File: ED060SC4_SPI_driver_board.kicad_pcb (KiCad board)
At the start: 4 copper layers, 71.2 x 49 mm, 82 parts, among them J1 ED060SC4, J2 Conn_01x06, J3 Conn_01x04, J4 Conn_01x04, J5 Conn_01x06, J6 Conn_01x02, SW1 SS12D07VG2, SW2 DSIC01LSGET, U1 TPS65185RGZR, U2 STM32F103C8T6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

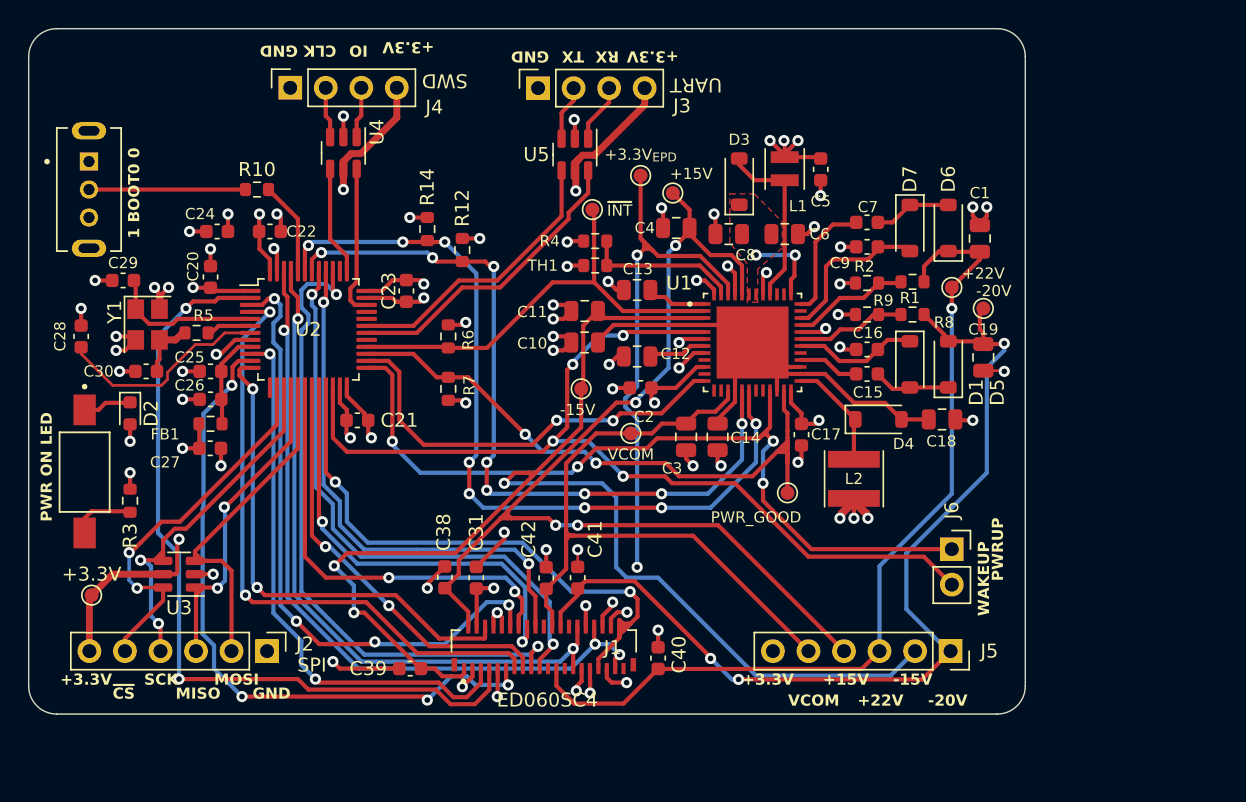
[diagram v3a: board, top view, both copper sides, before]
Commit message: Updated TPS pad for heat dissipation
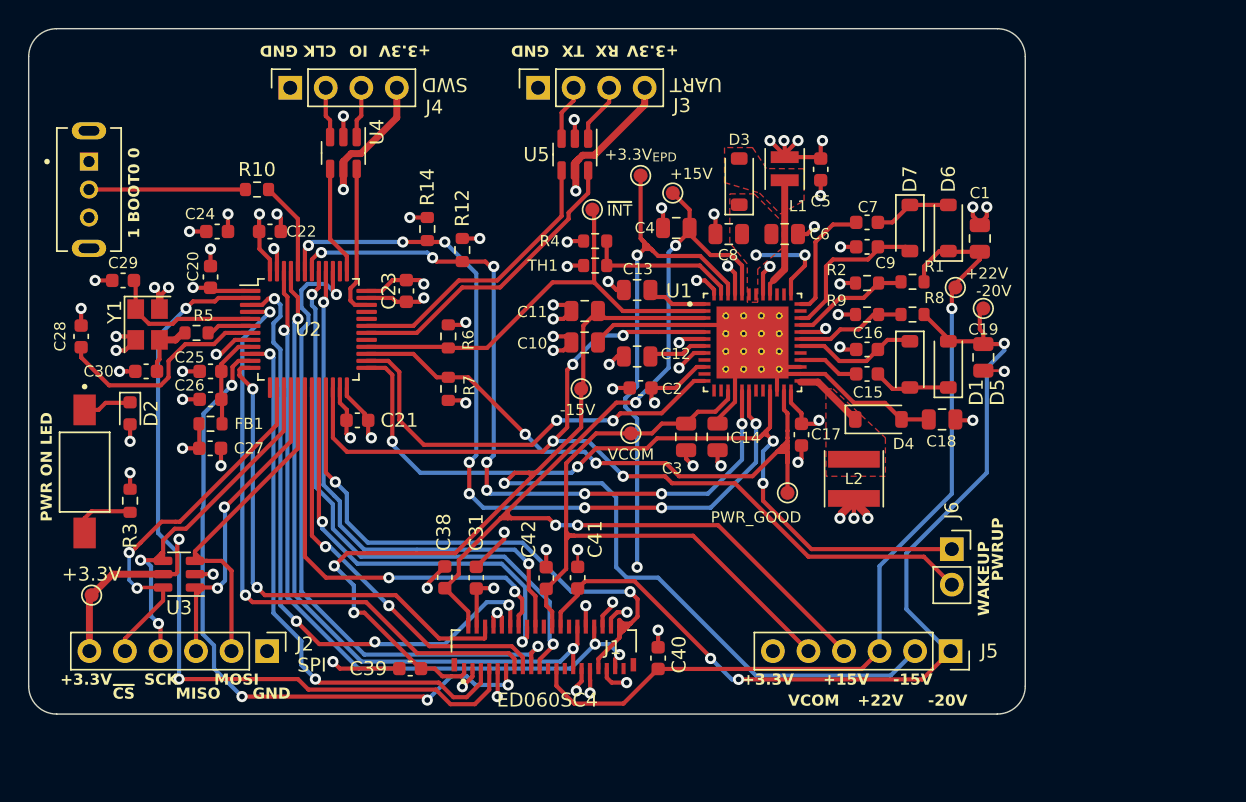
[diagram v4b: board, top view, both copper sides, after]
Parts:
- moved TP5 0.25 mm to (114.2, 65.5)
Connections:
- net /PWR_ON_LED renamed /PWR_ON_LED_0
- net Net-(R3-Pad1) renamed /PWR_ON_LED_1
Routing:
- net /EPD Power Rails/VB_SW: track 12.8 -> 8.60 mm
- net /EPD Power Rails/VN_SW: track 7.95 -> 5.16 mm
- net +3.3V: track 80.1 -> 81.4 mm, vias 20 -> 21
- net /EPD Power Rails/VB: track 5.74 -> 6.73 mm
- net /NRST: track 15.3 -> 15.9 mm
- net GND: track 106.4 -> 107.0 mm
- added copper zone on F.Cu, net /EPD Power Rails/VB_SW
- added copper zone on F.Cu, net /EPD Power Rails/VN_SW

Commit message: Smaller board outline and some silkscreen info
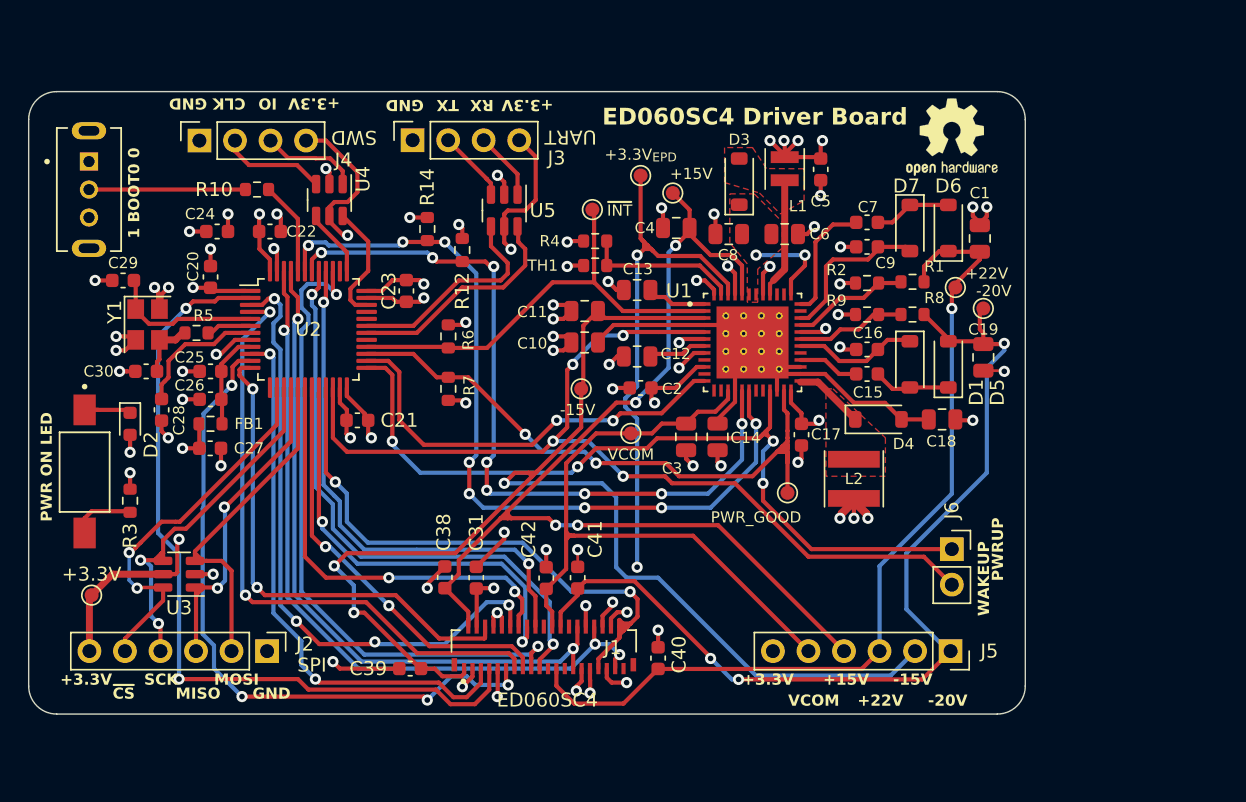
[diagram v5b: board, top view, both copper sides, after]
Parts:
- added REF**: OSHW-Logo2_7.3x6mm_SilkScreen, Symbol:OSHW-Logo2_7.3x6mm_SilkScreen, F.Cu at (114.0, 54.8)
- moved J3 9.72 mm to (75.5, 55.0)
- moved C28 7.79 mm to (57.5, 74.2), turned to 90 degrees
- moved J4 7.51 mm to (60.2, 55.0)
- moved U5 6.44 mm to (82.0, 60.0)
- moved U4 3.51 mm to (69.5, 59.2)
- moved D2 0.75 mm to (55.2, 75.2)
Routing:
- net /NRST: track 15.9 -> 9.60 mm
- net /USART1_RX: track 21.9 -> 16.4 mm
- net /USART1_TX: track 20.5 -> 15.5 mm
- net /SWCLK_conn: track 3.65 -> 7.53 mm
- net /SWDIO_conn: track 3.66 -> 7.00 mm
- net /SWCLK: track 7.81 -> 4.86 mm
- net /SWDIO: track 10.9 -> 8.60 mm
- net /USART1_TX_conn: track 3.97 -> 5.15 mm
- net +3.3V: track 81.4 -> 82.6 mm
- net /PWR_ON_LED_0: track 3.47 -> 4.33 mm
- net /USART1_RX_conn: track 4.23 -> 4.89 mm
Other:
- board size 71.2 x 49 mm -> 71.2 x 44.5 mm
- board text added: "ED060SC4 Driver Board"
- board text added: "Revision 1"
- board text added: "design by hatrix"

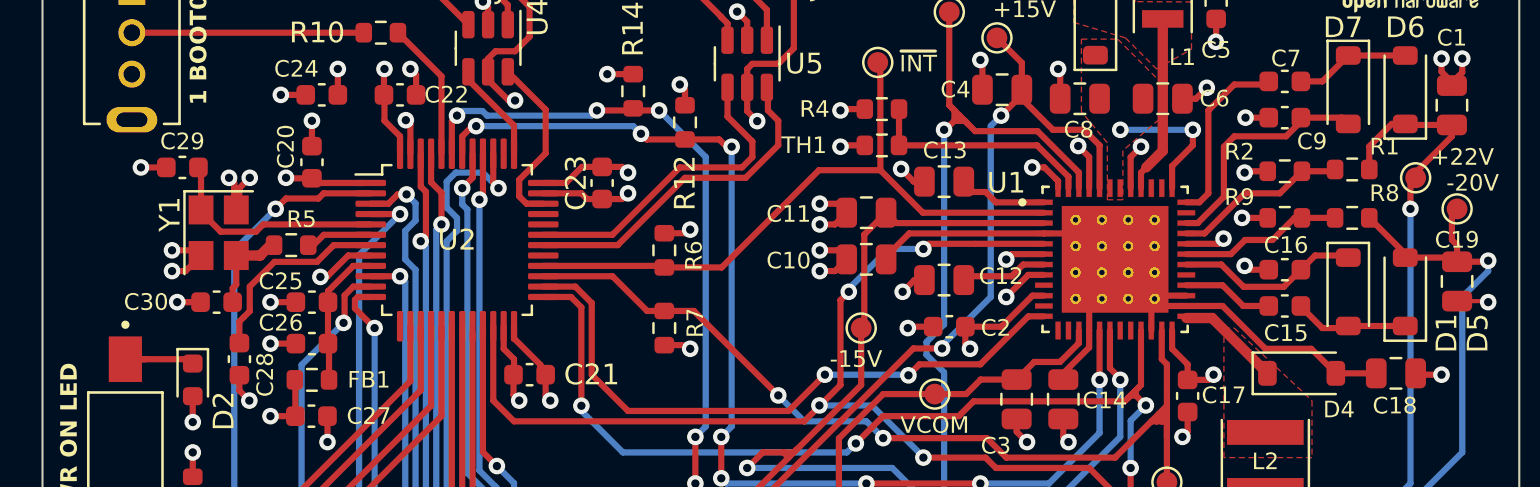
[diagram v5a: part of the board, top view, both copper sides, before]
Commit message: bigger via holes for TPS heat
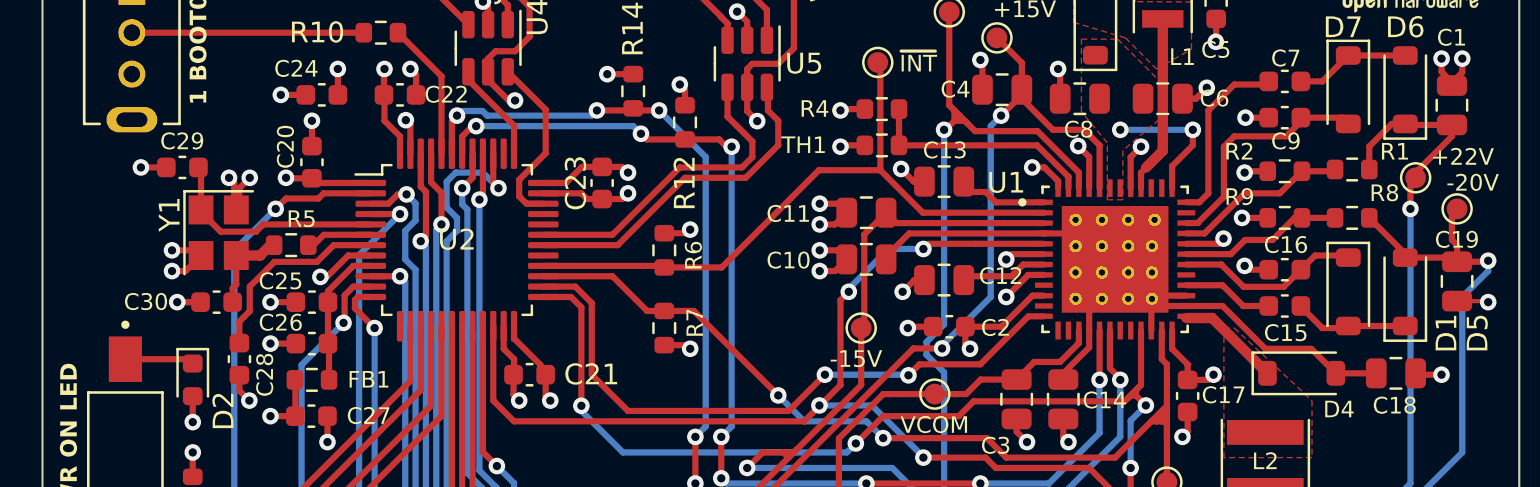
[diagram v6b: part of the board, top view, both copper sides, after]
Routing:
- net /PWR_ON_LED_0: track 4.33 -> 3.34 mm
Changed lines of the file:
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@@
     (pad "48" smd roundrect (at -2.75 -3.435 90) (size 0.86 0.26) (layers "F.Cu" "F.Paste" "F.Mask") (roundrect_rratio 0.03)
       (net 1 "GND") (pinfunction "AGND2") (pintype "power_in"))
-    (pad "49" thru_hole circle (at -1.905 -1.905) (size 0.508 0.508) (drill 0.254) (layers "*.Cu" "*.Mask")
+    (pad "49" thru_hole circle (at -1.905 -1.905) (size 0.6 0.6) (drill 0.3) (layers "*.Cu" "*.Mask")
       (net 77 "/EPD Power Rails/VN") (pinfunction "SUBSTRATE") (pintype "bidirectional"))
-    (pad "49" thru_hole circle (at -1.905 -0.635) (size 0.508 0.508) (drill 0.254) (layers "*.Cu" "*.Mask")
+    (pad "49" thru_hole circle (at -1.905 -0.635) (size 0.6 0.6) (drill 0.3) (layers "*.Cu" "*.Mask")
       (net 77 "/EPD Power Rails/VN") (pinfunction "SUBSTRATE") (pintype "bidirectional"))
-    (pad "49" thru_hole circle (at -1.905 0.635) (size 0.508 0.508) (drill 0.254) (layers "*.Cu" "*.Mask")
+    (pad "49" thru_hole circle (at -1.905 0.635) (size 0.6 0.6) (drill 0.3) (layers "*.Cu" "*.Mask")
       (net 77 "/EPD Power Rails/VN") (pinfunction "SUBSTRATE") (pintype "bidirectional"))
-    (pad "49" thru_hole circle (at -1.905 1.905) (size 0.508 0.508) (drill 0.254) (layers "*.Cu" "*.Mask")
+    (pad "49" thru_hole circle (at -1.905 1.905) (size 0.6 0.6) (drill 0.3) (layers "*.Cu" "*.Mask")
       (net 77 "/EPD Power Rails/VN") (pinfunction "SUBSTRATE") (pintype "bidirectional"))
-    (pad "49" thru_hole circle (at -0.635 -1.905) (size 0.508 0.508) (drill 0.254) (layers "*.Cu" "*.Mask")
+    (pad "49" thru_hole circle (at -0.635 -1.905) (size 0.6 0.6) (drill 0.3) (layers "*.Cu" "*.Mask")
       (net 77 "/EPD Power Rails/VN") (pinfunction "SUBSTRATE") (pintype "bidirectional"))
-    (pad "49" thru_hole circle (at -0.635 -0.635) (size 0.508 0.508) (drill 0.254) (layers "*.Cu" "*.Mask")
+    (pad "49" thru_hole circle (at -0.635 -0.635) (size 0.6 0.6) (drill 0.3) (layers "*.Cu" "*.Mask")
       (net 77 "/EPD Power Rails/VN") (pinfunction "SUBSTRATE") (pintype "bidirectional"))
-    (pad "49" thru_hole circle (at -0.635 0.635) (size 0.508 0.508) (drill 0.254) (layers "*.Cu" "*.Mask")
+    (pad "49" thru_hole circle (at -0.635 0.635) (size 0.6 0.6) (drill 0.3) (layers "*.Cu" "*.Mask")
       (net 77 "/EPD Power Rails/VN") (pinfunction "SUBSTRATE") (pintype "bidirectional"))
-    (pad "49" thru_hole circle (at -0.635 1.905) (size 0.508 0.508) (drill 0.254) (layers "*.Cu" "*.Mask")
+    (pad "49" thru_hole circle (at -0.635 1.905) (size 0.6 0.6) (drill 0.3) (layers "*.Cu" "*.Mask")
       (net 77 "/EPD Power Rails/VN") (pinfunction "SUBSTRATE") (pintype "bidirectional"))
     (pad "49" smd rect (at 0 0) (size 5.15 5.15) (layers "F.Cu" "F.Mask")
       (net 77 "/EPD Power Rails/VN") (pinfunction "SUBSTRATE") (pintype "bidirectional"))
-    (pad "49" thru_hole circle (at 0.635 -1.905) (size 0.508 0.508) (drill 0.254) (layers "*.Cu" "*.Mask")
+    (pad "49" thru_hole circle (at 0.635 -1.905) (size 0.6 0.6) (drill 0.3) (layers "*.Cu" "*.Mask")
       (net 77 "/EPD Power Rails/VN") (pinfunction "SUBSTRATE") (pintype "bidirectional"))
-    (pad "49" thru_hole circle (at 0.635 -0.635) (size 0.508 0.508) (drill 0.254) (layers "*.Cu" "*.Mask")
+    (pad "49" thru_hole circle (at 0.635 -0.635) (size 0.6 0.6) (drill 0.3) (layers "*.Cu" "*.Mask")
       (net 77 "/EPD Power Rails/VN") (pinfunction "SUBSTRATE") (pintype "bidirectional"))
-    (pad "49" thru_hole circle (at 0.635 0.635) (size 0.508 0.508) (drill 0.254) (layers "*.Cu" "*.Mask")
+    (pad "49" thru_hole circle (at 0.635 0.635) (size 0.6 0.6) (drill 0.3) (layers "*.Cu" "*.Mask")
       (net 77 "/EPD Power Rails/VN") (pinfunction "SUBSTRATE") (pintype "bidirectional"))
-    (pad "49" thru_hole circle (at 0.635 1.905) (size 0.508 0.508) (drill 0.254) (layers "*.Cu" "*.Mask")
+    (pad "49" thru_hole circle (at 0.635 1.905) (size 0.6 0.6) (drill 0.3) (layers "*.Cu" "*.Mask")
       (net 77 "/EPD Power Rails/VN") (pinfunction "SUBSTRATE") (pintype "bidirectional"))
-    (pad "49" thru_hole circle (at 1.905 -1.905) (size 0.508 0.508) (drill 0.254) (layers "*.Cu" "*.Mask")
+    (pad "49" thru_hole circle (at 1.778 -0.635) (size 0.6 0.6) (drill 0.3) (layers "*.Cu" "*.Mask")
       (net 77 "/EPD Power Rails/VN") (pinfunction "SUBSTRATE") (pintype "bidirectional"))
-    (pad "49" thru_hole circle (at 1.905 -0.635) (size 0.508 0.508) (drill 0.254) (layers "*.Cu" "*.Mask")
+    (pad "49" thru_hole circle (at 1.778 0.635) (size 0.6 0.6) (drill 0.3) (layers "*.Cu" "*.Mask")
       (net 77 "/EPD Power Rails/VN") (pinfunction "SUBSTRATE") (pintype "bidirectional"))
-    (pad "49" thru_hole circle (at 1.905 0.635) (size 0.508 0.508) (drill 0.254) (layers "*.Cu" "*.Mask")
+    (pad "49" thru_hole circle (at 1.778 1.905) (size 0.6 0.6) (drill 0.3) (layers "*.Cu" "*.Mask")
       (net 77 "/EPD Power Rails/VN") (pinfunction "SUBSTRATE") (pintype "bidirectional"))
-    (pad "49" thru_hole circle (at 1.905 1.905) (size 0.508 0.508) (drill 0.254) (layers "*.Cu" "*.Mask")
+    (pad "49" thru_hole circle (at 1.905 -1.905) (size 0.6 0.6) (drill 0.3) (layers "*.Cu" "*.Mask")
       (net 77 "/EPD Power Rails/VN") (pinfunction "SUBSTRATE") (pintype "bidirectional"))
     (model "./3d_models/TPS65185RGZR.step"
@@
     (property "ki_keywords" "cap capacitor")
     (attr smd)
-    (fp_text reference "C9" (at 1.311248 1.151252) (layer "F.SilkS")
+    (fp_text reference "C9" (at 0.061248 1.151252) (layer "F.SilkS")
         (effects (font (size 0.8 0.8) (thickness 0.15)))
     )
@@
     (property "ki_keywords" "R res resistor")
     (attr smd)
-    (fp_text reference "R1" (at 1.561248 -1.098748) (layer "F.SilkS")
+    (fp_text reference "R1" (at 2.061248 -0.848748) (layer "F.SilkS")
         (effects (font (size 0.8 0.8) (thickness 0.15)))
     )
@@
   (segment (start 55.0407 74.2532) (end 52 74.2532) (width 0.3) (layer "F.Cu") (net 15))
   (segment (start 55.25 74.4625) (end 55.0407 74.2532) (width 0.3) (layer "F.Cu") (net 15))
-  (segment (start 52 74.2532) (end 52.9968 74.2532) (width 0.3) (layer "F.Cu") (net 15))
   (segment (start 102.05 57.835) (end 102.05 64.2) (width 0.5) (layer "F.Cu") (net 16))
   (segment (start 101.25 65) (end 101 65.25) (width 0.3) (layer "F.Cu") (net 16))

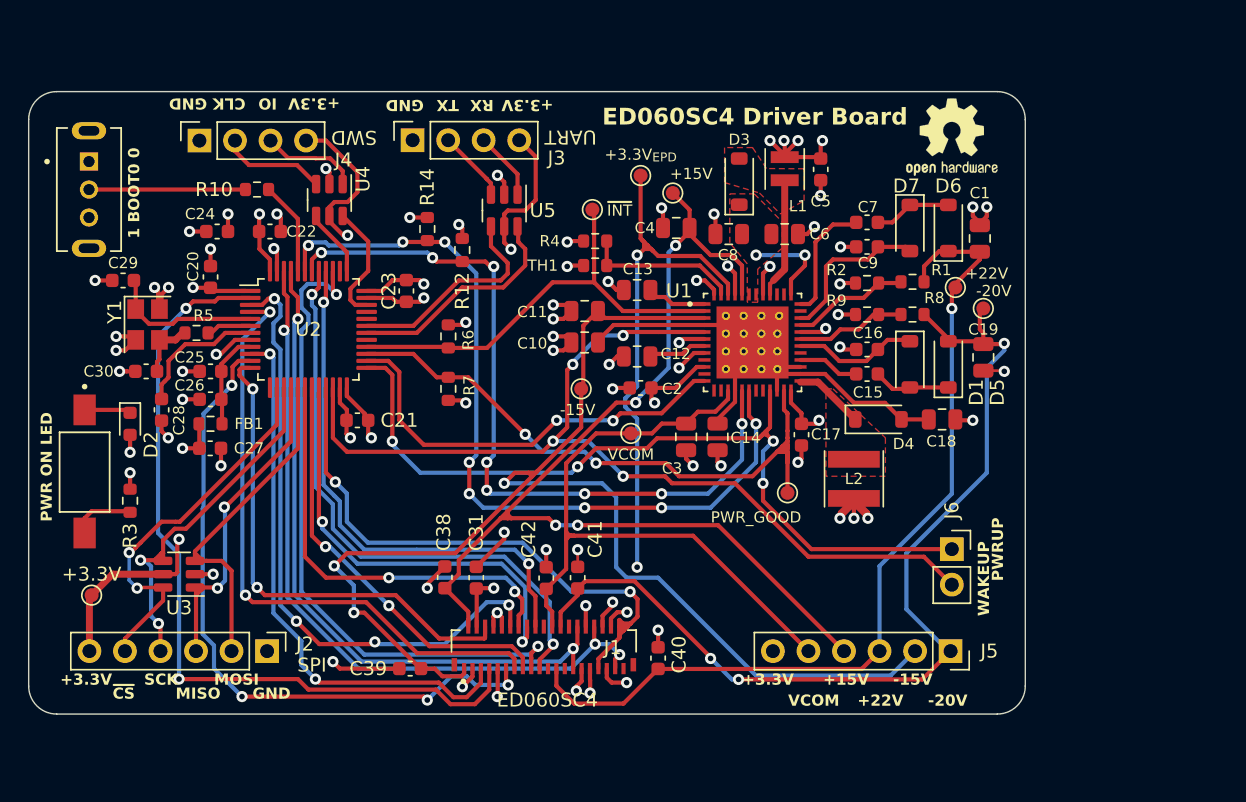
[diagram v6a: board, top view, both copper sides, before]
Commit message: Add ground pour to external layers
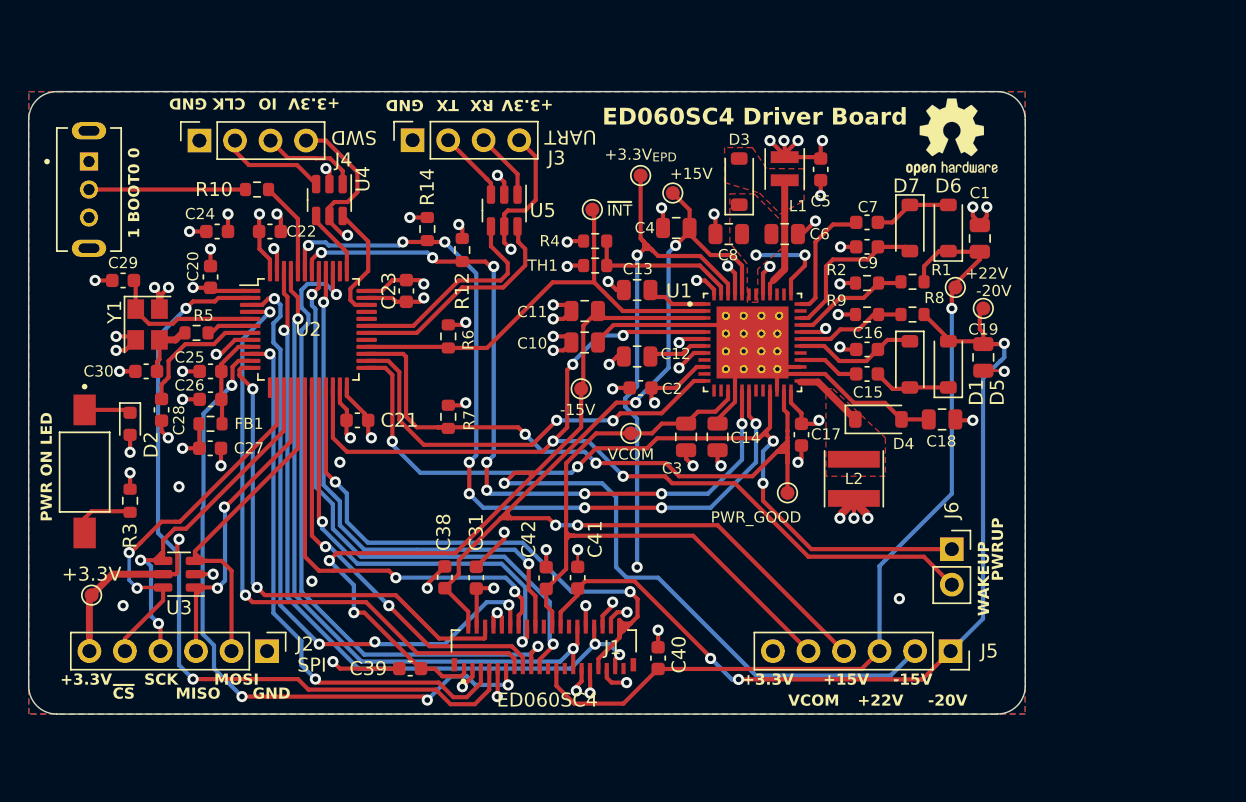
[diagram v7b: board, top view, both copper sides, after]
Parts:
- moved R7 2.00 mm to (78.0, 74.8), turned to -90 degrees
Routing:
- net /TPS_PWRGOOD: track 44.8 -> 48.1 mm
- net -20V: track 69.6 -> 66.9 mm
- net -15V: track 94.3 -> 95.0 mm
- net /EPD_OE: track 57.7 -> 57.1 mm
- net GND: track 107.2 -> 107.5 mm, vias 63 -> 68
- added copper zone on B.Cu, net GND
- added copper zone on F.Cu, net GND
